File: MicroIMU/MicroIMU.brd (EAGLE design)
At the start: 7.6 x 19.1 mm, 18 parts, among them IC1 LSM303DLHC

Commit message: Done routing
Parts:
- removed 15V: 15V, wirepad:1,6/0,8
- added +15V: 15V, wirepad:1,6/0,8
- moved C7 10.2 mm to (6.86, 16.3), turned to 270 degrees
- moved C8 8.57 mm to (3.05, 16.3), turned to 270 degrees
- moved C2 8.35 mm to (6.60, 7.49), turned to 90 degrees
- moved U$2 8.35 mm to (4.95, 16.3), turned to 180 degrees
- moved GND 8.03 mm to (1.52, 15.5)
- moved SDA 7.82 mm to (1.52, 6.35)
- moved C4 7.33 mm to (4.83, 9.14), turned to 0 degrees
- moved C9 7.31 mm to (2.79, 9.14)
- moved R2 6.19 mm to (2.79, 12.4), turned to 0 degrees
- moved SCL 5.23 mm to (1.52, 8.13)
- moved C1 3.56 mm to (1.78, 3.81), turned to 180 degrees
- moved IC1 3.18 mm to (4.57, 5.84), turned to 270 degrees
- moved U$1 2.84 mm to (5.08, 11.4)
- moved R1 2.43 mm to (2.41, 11.2)
- moved C6 2.30 mm to (4.32, 13.7), turned to 90 degrees
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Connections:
- net +15V: now also +15V.1; no longer 15V.1
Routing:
- net SDA: track 0.00 -> 14.7 mm, vias 0 -> 1
- net SCL: track 0.00 -> 10.3 mm
- net +3V3: track 10.4 -> 15.7 mm, vias 0 -> 3
- net +15V: track 2.06 -> 4.14 mm
- net N$9: track 1.93 -> 1.27 mm
- net GND: track 31.0 -> 30.8 mm, vias 0 -> 5
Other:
- board size 7.6 x 19.1 mm -> 7.6 x 18 mm

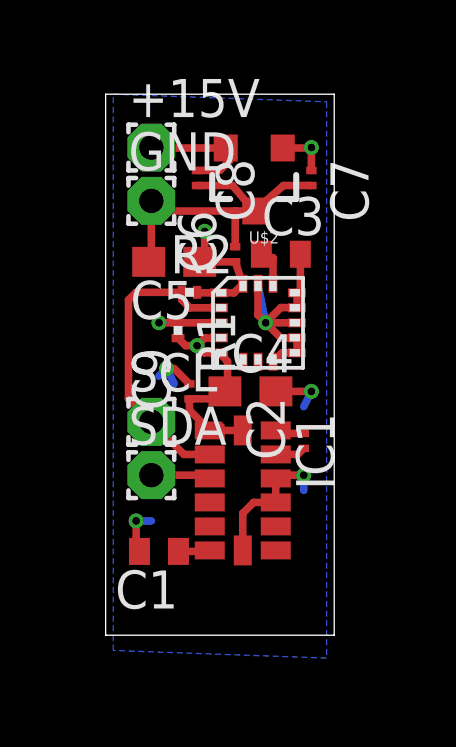
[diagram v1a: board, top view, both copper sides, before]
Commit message: Galen made minor layout changes to save space
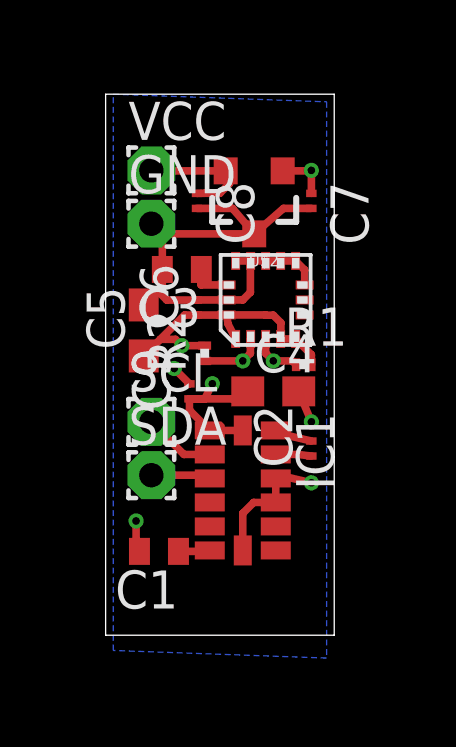
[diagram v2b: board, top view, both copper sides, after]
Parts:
- removed +15V: 15V, wirepad:1,6/0,8
- added VCC: VCC, wirepad:1,6/0,8
- moved R1 4.34 mm to (6.60, 10.0), turned to 0 degrees
- moved C3 3.34 mm to (2.54, 13.2), turned to 180 degrees
- moved C5 2.50 mm to (1.27, 11.2), turned to 90 degrees
- moved C6 2.18 mm to (3.05, 11.9)
- moved R2 2.09 mm to (3.30, 10.4), turned to 90 degrees
- moved U$1 0.80 mm to (5.33, 12.2), turned to 90 degrees
- moved C4 0.76 mm to (5.59, 9.14)
- moved C7 0.76 mm to (6.86, 15.5)
- moved C8 0.76 mm to (3.05, 15.5)
- moved GND 0.76 mm to (1.52, 14.7)
- moved U$2 0.76 mm to (4.95, 15.5)
- moved C2 0.36 mm to (6.86, 7.24)
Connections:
- removed net +15V: +15V.1, C8.1, U$2.2
- new net VCC: C8.1, U$2.2, VCC.1
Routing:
- net GND: track 30.8 -> 26.2 mm, vias 5 -> 4
- net VCC: track 0.00 -> 4.14 mm
- net +15V: track 4.14 -> 0.00 mm
- net +3V3: track 15.7 -> 19.6 mm
- net SDA: track 14.7 -> 11.6 mm
- net SCL: track 10.3 -> 9.20 mm, vias 0 -> 1

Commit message: Added labels to silkscreen layer
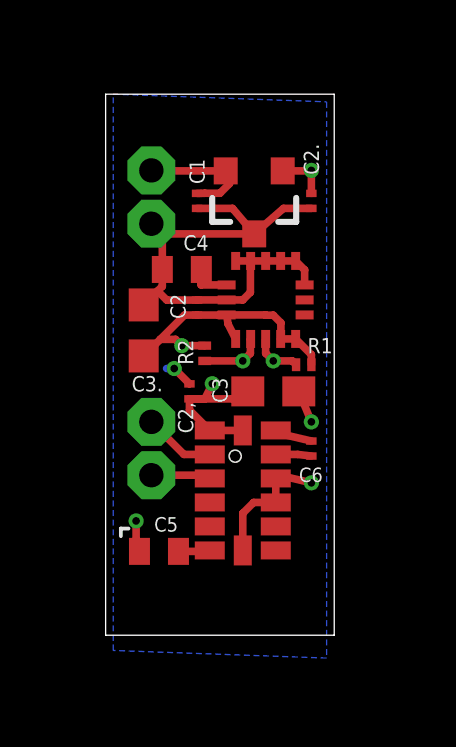
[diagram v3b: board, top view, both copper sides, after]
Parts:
- removed C8: 0.1uF, resistor:C0201
- added C3.: 10uF, resistor:C0603
- C1: value 4.7uF -> 0.1uF; device resistor:C0402 -> resistor:C0201
- C2: value 0.22 uF -> 0.1uF
- C3: value 0.01 uF -> 10uF; device resistor:C0402 -> resistor:C0603
- C4: value 10uF -> 0.01 uF; device resistor:C0603 -> resistor:C0402
- C5: value 10uF -> 4.7uF; device resistor:C0603 -> resistor:C0402
- C6: value 0.1uF -> 0.22 uF
- VIN: value VCC -> 15V
- moved C1 11.8 mm to (3.05, 15.5), turned to 270 degrees
- moved C5 7.38 mm to (1.78, 3.81), turned to 180 degrees
- moved C2 6.05 mm to (3.05, 11.9)
- moved C6 6.05 mm to (6.86, 7.24)
- moved C3 5.08 mm to (5.59, 9.14), turned to 0 degrees
- moved C4 5.08 mm to (2.54, 13.2), turned to 180 degrees
- renumbered C7 to C2., C9 to C2,, VCC to VIN
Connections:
- removed net VCC: C8.1, U$2.2, VIN.1
- new net +15V: C1.1, U$2.2, VIN.1
- net +3V3: now also C2.1, C3..1, C3.1; no longer C4.1, C5.1, C6.1
- net GND: now also C2.2, C3..2; no longer C6.2, C8.2
- net N$1: now also C5.1; no longer C1.1
- net N$2: now also C6.1; no longer C2.1
- net N$3: now also C6.2; no longer C2.2
- net N$9: now also C4.1; no longer C3.1
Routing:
- net +15V: track 0.00 -> 4.61 mm
- net VCC: track 4.14 -> 0.00 mm
- net +3V3: track 19.6 -> 19.1 mm

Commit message: Improved silkscreen labels
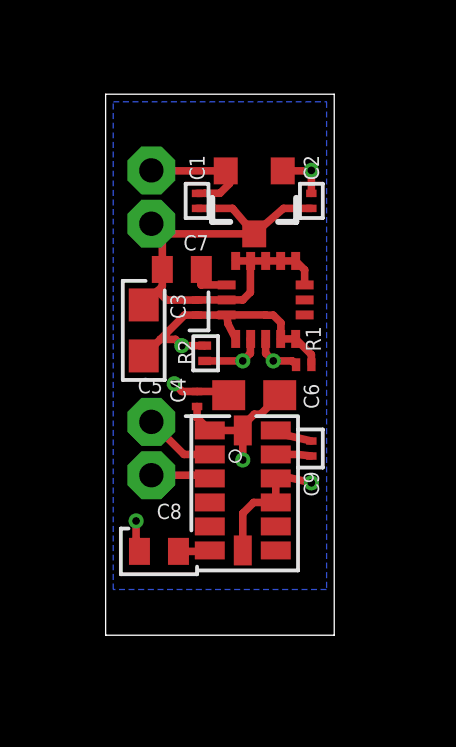
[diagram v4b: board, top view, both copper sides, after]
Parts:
- removed C2,, C2.: 0.1uF, resistor:C0201
- removed C3.: 10uF, resistor:C0603
- added C7: 0.01 uF, resistor:C0402
- added C8: 4.7uF, resistor:C0402
- added C9: 0.22 uF, resistor:C0201
- C3: value 10uF -> 0.1uF; device resistor:C0603 -> resistor:C0201
- C4: value 0.01 uF -> 0.1uF; device resistor:C0402 -> resistor:C0201
- C5: value 4.7uF -> 10uF; device resistor:C0402 -> resistor:C0603
- C6: value 0.22 uF -> 10uF; device resistor:C0201 -> resistor:C0603
- moved C5 7.38 mm to (1.27, 11.2), turned to 90 degrees
- moved C2 5.21 mm to (6.86, 15.5), turned to 270 degrees
- moved C4 4.35 mm to (3.05, 8.89), turned to 90 degrees
- moved C3 3.78 mm to (3.05, 11.9), turned to 90 degrees
- moved C6 2.61 mm to (4.95, 9.02), turned to 180 degrees
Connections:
- net +3V3: now also C4.1, C5.1, C6.1; no longer C2,.1, C2..1, C3..1
- net GND: now also C6.2, C7.2, C8.2; no longer C2,.2, C2..2, C3..2
- net N$1: now also C8.1; no longer C5.1
- net N$2: now also C9.1; no longer C6.1
- net N$3: now also C9.2; no longer C6.2
- net N$9: now also C7.1; no longer C4.1
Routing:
- net +3V3: track 19.1 -> 17.7 mm
- net GND: track 26.2 -> 26.1 mm, vias 4 -> 3

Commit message: Galen rearranged the board again - rotated the LSM303DLHC by 90 degrees
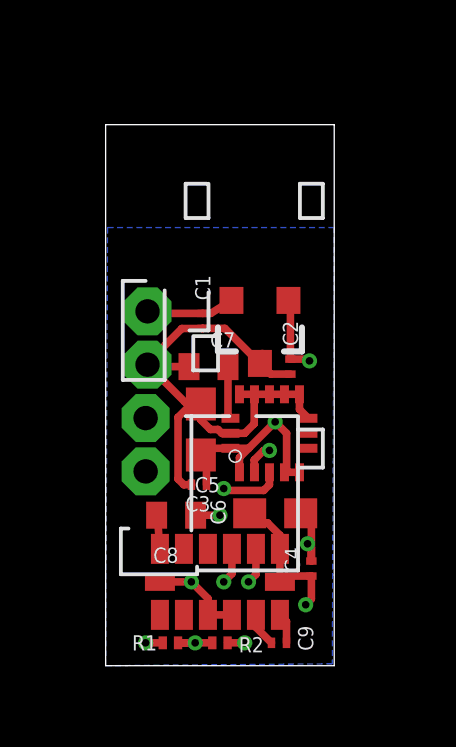
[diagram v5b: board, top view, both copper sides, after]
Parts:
- moved R1 10.3 mm to (2.16, 0.76)
- moved R2 9.67 mm to (3.81, 0.76), turned to 180 degrees
- moved C4 6.82 mm to (6.86, 3.24)
- moved C9 6.57 mm to (5.78, 0.76), turned to 0 degrees
- moved C3 5.91 mm to (3.11, 6.03), turned to 180 degrees
- moved C2 5.57 mm to (6.16, 9.97)
- moved VIN 4.70 mm to (1.40, 11.8)
- moved GND 4.70 mm to (1.40, 10.0)
- moved U$1 4.45 mm to (5.46, 7.75)
- moved U$2 4.32 mm to (5.14, 11.2)
- moved C1 4.01 mm to (3.24, 11.5)
- moved C6 4.00 mm to (5.65, 5.08), turned to 0 degrees
- moved C5 3.81 mm to (3.17, 7.87)
- moved C7 3.36 mm to (3.43, 9.97)
- moved IC1 3.14 mm to (3.81, 2.79), turned to 180 degrees
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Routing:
- net SDA: track 11.6 -> 17.1 mm, vias 1 -> 3
- net SCL: track 9.20 -> 14.1 mm, vias 1 -> 3
- net +15V: track 4.61 -> 2.99 mm
- net GND: track 26.1 -> 27.0 mm
- net +3V3: vias 3 -> 4

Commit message: More rearrangement by Galen - everything is much closer together now
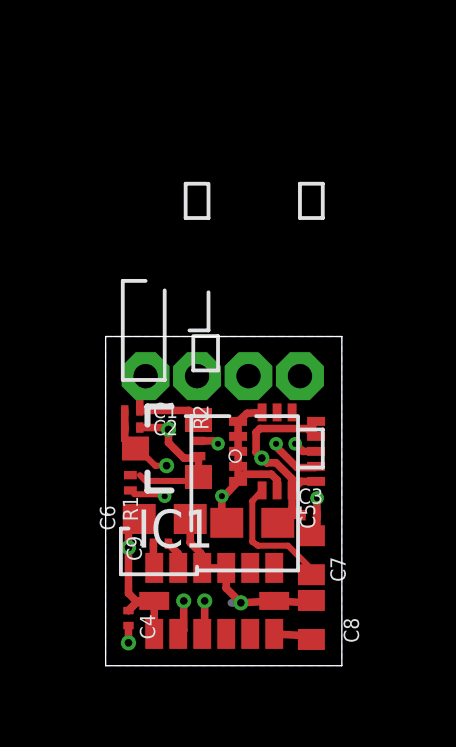
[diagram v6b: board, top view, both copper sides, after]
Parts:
- moved C7 7.16 mm to (6.86, 3.68), turned to 90 degrees
- moved R2 6.51 mm to (3.11, 7.24), turned to 270 degrees
- moved C4 6.32 mm to (0.76, 1.59), turned to 270 degrees
- moved SDA 6.04 mm to (6.48, 9.65)
- moved C8 5.70 mm to (6.86, 1.52), turned to 90 degrees
- moved C2 5.65 mm to (0.89, 7.94), turned to 180 degrees
- moved R1 5.50 mm to (0.83, 6.10), turned to 90 degrees
- moved C9 5.14 mm to (1.84, 4.06), turned to 180 degrees
- moved U$2 4.98 mm to (2.10, 7.24), turned to 90 degrees
- moved C3 3.82 mm to (6.79, 5.02), turned to 0 degrees
- moved C1 3.80 mm to (0.89, 8.51), turned to 180 degrees
- moved SCL 3.70 mm to (4.76, 9.65)
- moved C6 3.69 mm to (1.97, 4.89)
- moved C5 3.55 mm to (4.89, 4.76), turned to 180 degrees
- moved VIN 2.16 mm to (1.33, 9.65)
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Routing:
- net GND: track 27.0 -> 17.8 mm, vias 3 -> 5
- net SDA: track 17.1 -> 14.1 mm
- net N$9: track 1.76 -> 4.36 mm
- net +3V3: track 17.7 -> 20.2 mm, vias 4 -> 3
- net SCL: track 14.1 -> 16.5 mm
- net +15V: track 2.99 -> 3.71 mm
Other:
- board size 7.6 x 18 mm -> 7.9 x 11 mm

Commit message: Galen switched to LSM303D for accelerometer/compass - newer design with smaller package
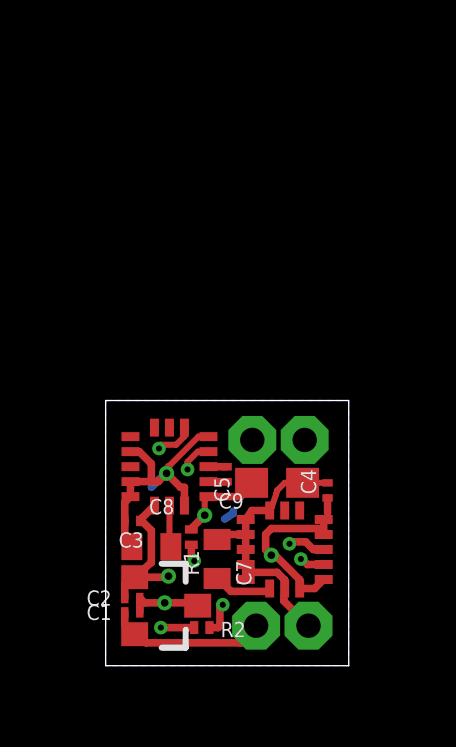
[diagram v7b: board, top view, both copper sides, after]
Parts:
- removed C6: 10uF, resistor:C0603
- removed IC1: LSM303DLHC, st-microelectronics:LGA-14
- added U$3: LSM303D, st:LGA16L
- moved GND 9.11 mm to (6.76, 1.33)
- moved VIN 9.10 mm to (5.02, 1.33)
- moved C4 7.88 mm to (7.40, 5.84), turned to 90 degrees
- moved C1 6.73 mm to (0.89, 1.78), turned to 0 degrees
- moved R2 5.97 mm to (3.21, 1.27), turned to 180 degrees
- moved C3 5.91 mm to (0.89, 4.83), turned to 180 degrees
- moved C8 5.87 mm to (1.52, 3.97), turned to 180 degrees
- moved C2 5.68 mm to (0.89, 2.25), turned to 0 degrees
- moved U$2 5.24 mm to (1.97, 2.00), turned to 270 degrees
- moved U$1 3.28 mm to (5.97, 3.87)
- moved C9 3.19 mm to (4.03, 6.38), turned to 270 degrees
- moved C7 3.15 mm to (3.71, 3.56)
- moved SCL 2.83 mm to (6.64, 7.52)
- moved R1 2.72 mm to (2.86, 4.29)
- moved SDA 2.65 mm to (4.89, 7.52)
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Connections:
- net +3V3: now also U$3.P$1, U$3.P$14; no longer C6.1, IC1.1, IC1.14
- net GND: now also U$3.P$10, U$3.P$12, U$3.P$13, U$3.P$16, U$3.P$5; no longer C6.2, IC1.10, IC1.11, IC1.7
- net N$1: now also U$3.P$15; no longer IC1.6
- net N$2: now also U$3.P$3; no longer IC1.12
- net N$3: now also U$3.P$2; no longer IC1.13
- net SCL: now also U$3.P$4; no longer IC1.2
- net SDA: now also U$3.P$6; no longer IC1.3
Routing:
- net GND: track 17.8 -> 22.4 mm, vias 5 -> 2
- net +3V3: track 20.2 -> 15.7 mm, vias 3 -> 4
- net N$9: track 4.36 -> 1.96 mm
- net +15V: track 3.71 -> 5.27 mm
- net SCL: track 16.5 -> 15.1 mm
- net SDA: track 14.1 -> 15.2 mm
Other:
- board size 7.9 x 11 mm -> 8.1 x 8.8 mm

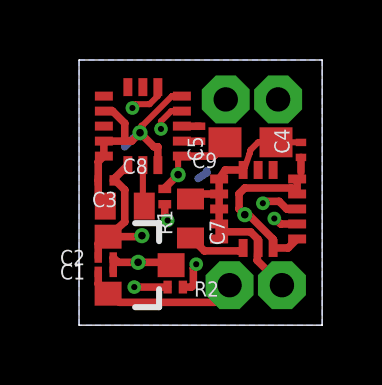
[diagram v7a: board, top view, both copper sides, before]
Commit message: Added missing connections for CS and SA0 on LSM303D
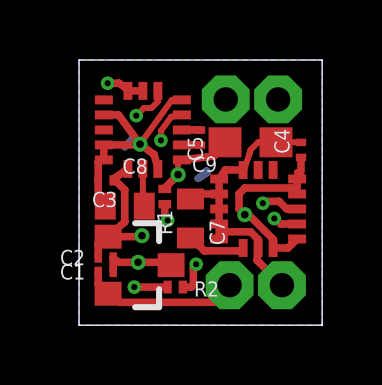
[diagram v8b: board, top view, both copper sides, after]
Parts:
- moved C9 0.13 mm to (4.03, 6.25)
- moved U$3 0.13 mm to (2.13, 6.51)
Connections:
- net +3V3: now also U$3.P$7, U$3.P$8
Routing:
- net +3V3: track 15.7 -> 17.3 mm, vias 4 -> 5
